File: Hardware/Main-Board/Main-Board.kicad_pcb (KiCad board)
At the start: 2 copper layers, 124.3 x 131.7 mm, 102 parts, among them J101 ProgrammCard, J102 MemoryCard, J103 Edge_Connector, J104 LCD_CON, J106 EXT_AUDIO, J107 MOUSE_PORT, J108 Voice_Board_Mock, Q101 C9012, U101 DMG CPU, U102 GM76C88LFW-15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

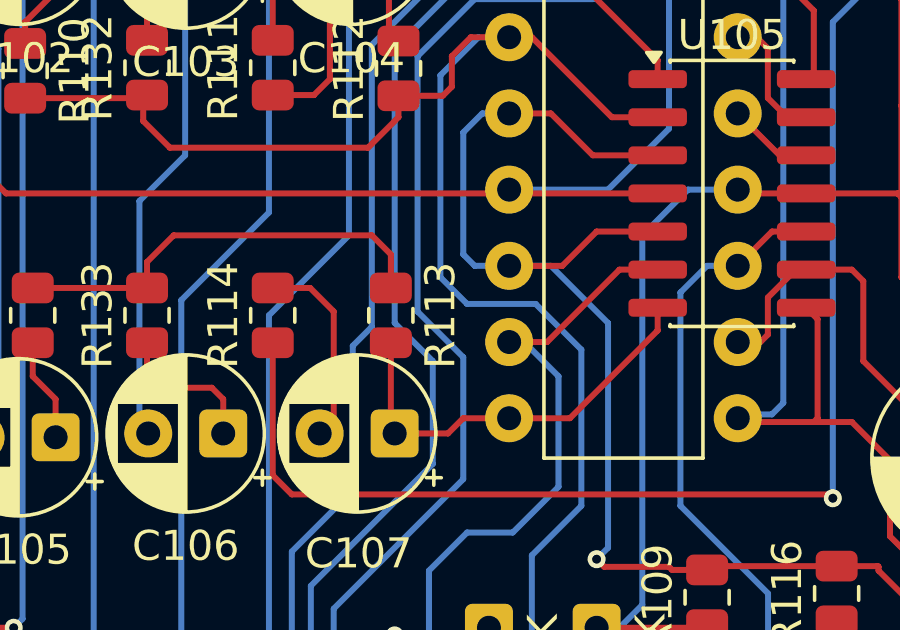
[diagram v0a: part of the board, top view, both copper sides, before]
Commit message: Fixed error in Audio-Mixer - Added more signal names
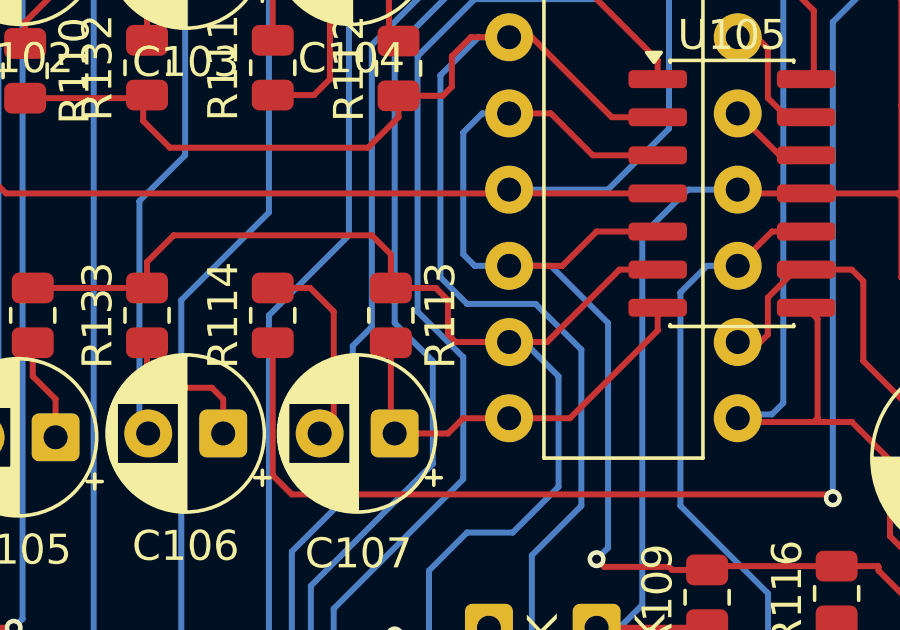
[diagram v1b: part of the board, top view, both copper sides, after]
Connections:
- net /DISP_10 renamed /ADUIO_OUT_2'
- net /DISP_12 renamed /AUDIO_OUT_1
- net /DISP_4 renamed /SPEAKER
- net /DISP_6 renamed /BATT_LOW
- net /EDGE_14 renamed /MONO_IN
- net /EDGE_21 renamed /LNK_ASIC_EN
- net /EDGE_22 renamed /VOICE_DATA
- net /EDGE_23 renamed /VOICE_~{RST}
- net /LNK_EN renamed /LNK_ASIC_EN'
- net /P14_EDGE renamed /P14_EXT
- FB108 pad 2: /DISP_8 -> /ADUIO_OUT_1'
- J103 pad 20: /LNK_EDGE_EN -> /LNK_EXT_EN
- J104 pad 14: /DISP_14 -> /ADUIO_OUT_2
- J104 pad 8: /DISP_8 -> /AUDIO_OUT_1'
- R111 pad 2: /DISP_14 -> /AUDIO_OUT_2
- R113 pad 1: Net-(R113-Pad1) -> /MC_?_4
- R115 pad 2: Net-(R113-Pad1) -> /MC_?_4
- R133 pad 2: Net-(R113-Pad1) -> /MC_?_4
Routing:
- net /DISP_14: track 48.8 -> 0.00 mm, vias 2 -> 0
- net /ADUIO_OUT_2: track 0.00 -> 48.8 mm, vias 0 -> 2
- net /DISP_8: track 22.3 -> 0.00 mm
- net /ADUIO_OUT_1': track 0.00 -> 22.3 mm
- net /MC_?_4: track 175.7 -> 195.6 mm
- net Net-(R113-Pad1): track 14.6 -> 0.00 mm
